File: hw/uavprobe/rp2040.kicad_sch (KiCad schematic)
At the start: 44 parts, among them IC1 UCLAMP3306P.TCT, SW1 SW_Push, U1 W25Q16JVSS, U2 NCP1117-5.0_SOT223, U3 RP2040, U4 TJA1051T-3, U5 TJA1051T-3, Y1 ABLS-12.000MHZ-B4-T

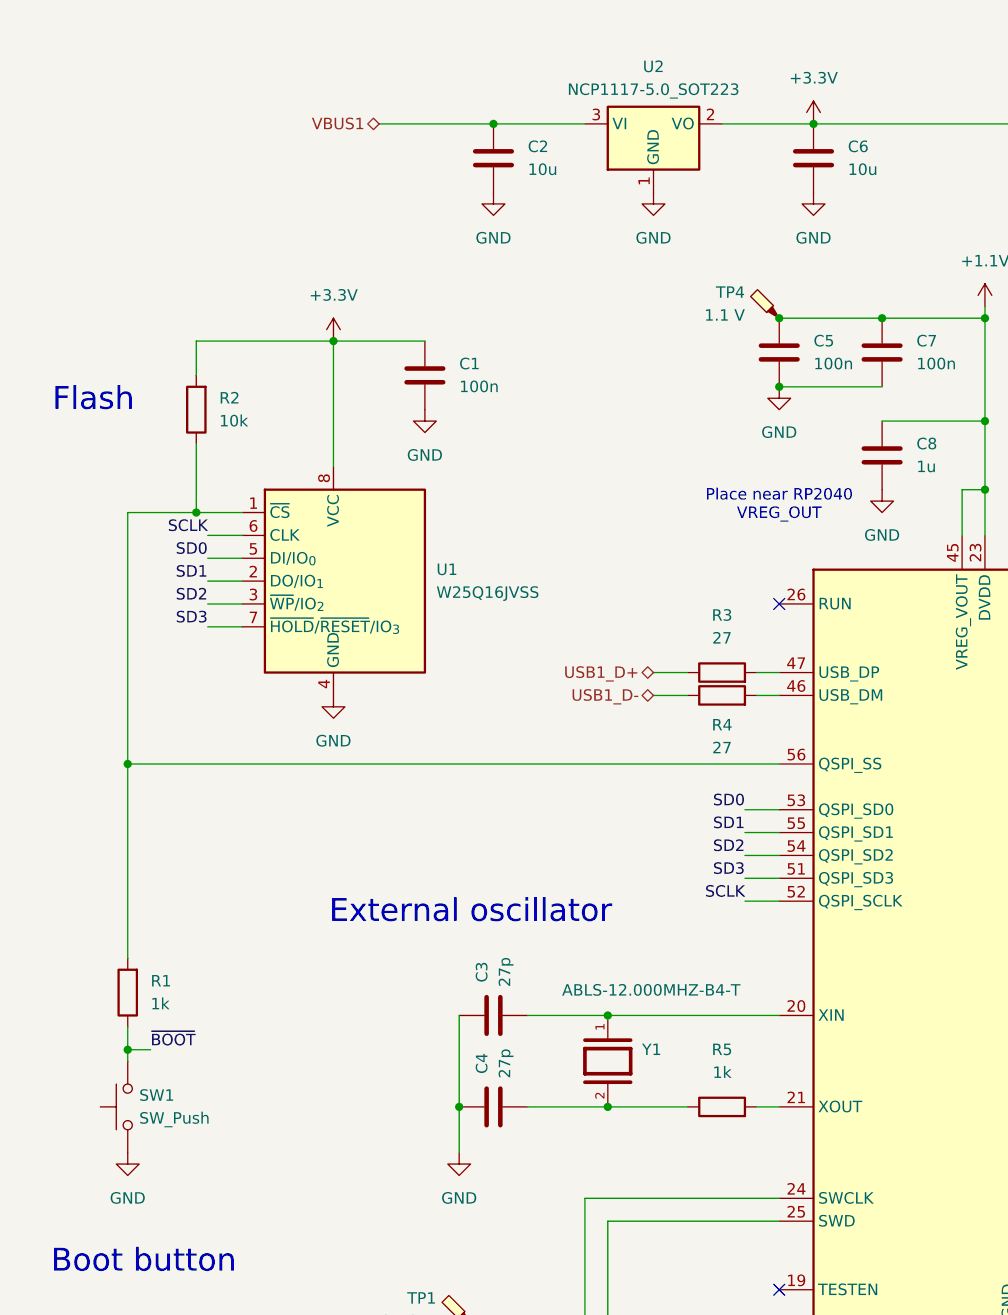
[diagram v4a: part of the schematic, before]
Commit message: ERC pass
Footprint and symbol copy editing warnings left
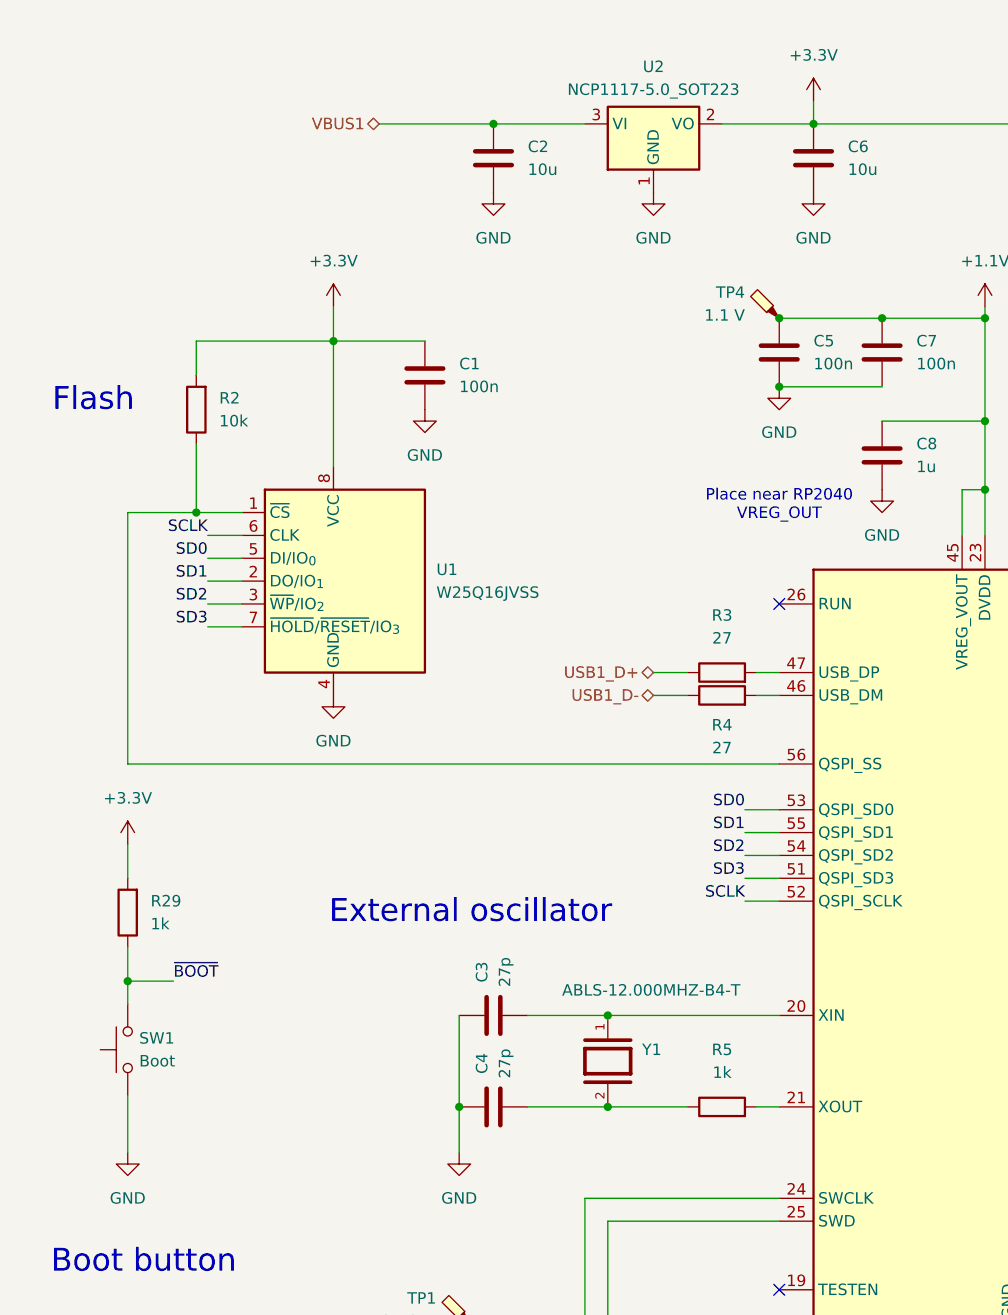
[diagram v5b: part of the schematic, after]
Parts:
- removed R1: 1k, symbol Device:R
- added R29: 1k, symbol Device:R
- SW1: value SW_Push -> Boot
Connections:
- net +3.3V: now also R29.2
- net ~{BOOT}: now also R29.1
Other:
- moved on the sheet: SW1
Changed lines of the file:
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@@
 	)
 	(junction
-		(at 25.4 99.06)
-		(diameter 0)
-		(color 0 0 0 0)
-	)
-	(junction
 		(at 120.65 68.58)
 		(diameter 0)
@@
 	)
 	(junction
+		(at 25.4 123.19)
+		(diameter 0)
+		(color 0 0 0 0)
+	)
+	(junction
 		(at 101.6 27.94)
 		(diameter 0)
@@
 	)
 	(junction
-		(at 25.4 130.81)
-		(diameter 0)
-		(color 0 0 0 0)
-	)
-	(junction
 		(at 151.13 57.15)
 		(diameter 0)
@@
 	(wire
 		(pts
-			(xy 25.4 130.81) (xy 25.4 132.08)
+			(xy 62.23 127) (xy 62.23 137.16)
 		)
 		(stroke
@@
 	(wire
 		(pts
-			(xy 62.23 127) (xy 62.23 137.16)
+			(xy 120.65 48.26) (xy 120.65 49.53)
 		)
 		(stroke
@@
 	(wire
 		(pts
-			(xy 120.65 48.26) (xy 120.65 49.53)
+			(xy 162.56 49.53) (xy 173.99 49.53)
 		)
 		(stroke
@@
 	(wire
 		(pts
-			(xy 162.56 49.53) (xy 173.99 49.53)
+			(xy 97.79 147.32) (xy 76.2 147.32)
 		)
 		(stroke
@@
 	(wire
 		(pts
-			(xy 97.79 147.32) (xy 76.2 147.32)
+			(xy 162.56 57.15) (xy 173.99 57.15)
 		)
 		(stroke
@@
 	(wire
 		(pts
-			(xy 25.4 99.06) (xy 25.4 120.65)
+			(xy 101.6 25.4) (xy 101.6 27.94)
 		)
 		(stroke
@@
 	(wire
 		(pts
-			(xy 162.56 57.15) (xy 173.99 57.15)
+			(xy 246.38 101.6) (xy 266.7 101.6)
 		)
 		(stroke
@@
 	(wire
 		(pts
-			(xy 246.38 101.6) (xy 266.7 101.6)
+			(xy 69.85 127) (xy 78.74 127)
 		)
 		(stroke
@@
 	(wire
 		(pts
-			(xy 69.85 127) (xy 78.74 127)
+			(xy 25.4 135.89) (xy 25.4 142.24)
 		)
 		(stroke
@@
 	(wire
 		(pts
+			(xy 48.26 48.26) (xy 48.26 52.07)
+		)
+		(stroke
+			(width 0)
+			(type default)
+		)
+	)
+	(wire
+		(pts
 			(xy 151.13 49.53) (xy 162.56 49.53)
 		)
@@
 	(wire
 		(pts
+			(xy 25.4 123.19) (xy 25.4 119.38)
+		)
+		(stroke
+			(width 0)
+			(type default)
+		)
+	)
+	(wire
+		(pts
+			(xy 25.4 111.76) (xy 25.4 107.95)
+		)
+		(stroke
+			(width 0)
+			(type default)
+		)
+	)
+	(wire
+		(pts
 			(xy 95.25 88.9) (xy 97.79 88.9)
 		)
@@
 	(wire
 		(pts
-			(xy 25.4 128.27) (xy 25.4 130.81)
-		)
-		(stroke
-			(width 0)
-			(type default)
-		)
-	)
-	(wire
-		(pts
 			(xy 196.85 137.16) (xy 201.93 137.16)
 		)
@@
 	(wire
 		(pts
-			(xy 27.94 130.81) (xy 25.4 130.81)
-		)
-		(stroke
-			(width 0)
-			(type default)
-		)
-	)
-	(wire
-		(pts
 			(xy 95.25 137.16) (xy 97.79 137.16)
 		)
@@
 	(wire
 		(pts
+			(xy 25.4 125.73) (xy 25.4 123.19)
+		)
+		(stroke
+			(width 0)
+			(type default)
+		)
+	)
+	(wire
+		(pts
 			(xy 241.3 86.36) (xy 246.38 86.36)
 		)
@@
 	(wire
 		(pts
+			(xy 25.4 123.19) (xy 30.48 123.19)
+		)
+		(stroke
+			(width 0)
+			(type default)
+		)
+	)
+	(wire
+		(pts
 			(xy 139.7 57.15) (xy 151.13 57.15)
 		)
@@
 		)
 	)
-	(label "~{BOOT}"
-		(at 27.94 130.81 0)
-		(effects
-			(font
-				(size 1.27 1.27)
-			)
-			(justify left bottom)
-		)
-	)
 	(label "SD0"
 		(at 34.29 76.2 180)
@@
 		)
 	)
+	(label "~{BOOT}"
+		(at 30.48 123.19 0)
+		(effects
+			(font
+				(size 1.27 1.27)
+			)
+			(justify left bottom)
+		)
+	)
 	(label "SD0"
 		(at 93.98 104.14 180)
@@
 	(symbol
 		(lib_id "power:+3.3V")
-		(at 48.26 52.07 0)
+		(at 48.26 48.26 0)
 		(unit 1)
 		(exclude_from_sim no)
@@
 		(fields_autoplaced yes)
 		(property "Reference" "#PWR02"
-			(at 48.26 55.88 0)
+			(at 48.26 52.07 0)
 			(effects
 				(font
@@
 		)
 		(property "Value" "+3.3V"
-			(at 48.26 46.99 0)
+			(at 48.26 43.18 0)
 			(effects
 				(font
@@
 		)
 		(property "Footprint" ""
-			(at 48.26 52.07 0)
+			(at 48.26 48.26 0)
 			(effects
 				(font
@@
 		)
 		(property "Datasheet" ""
-			(at 48.26 52.07 0)
+			(at 48.26 48.26 0)
 			(effects
 				(font
@@
 		)
 		(property "Description" "Power symbol creates a global label with name \"+3.3V\""
-			(at 48.26 52.07 0)
+			(at 48.26 48.26 0)
 			(effects
 				(font
@@
 	(symbol
 		(lib_id "power:+3.3V")
-		(at 101.6 27.94 0)
+		(at 101.6 25.4 0)
 		(unit 1)
 		(exclude_from_sim no)
@@
 		(dnp no)
 		(property "Reference" "#PWR010"
-			(at 101.6 31.75 0)
+			(at 101.6 29.21 0)
 			(effects
 				(font
@@
 		)
 		(property "Value" "+3.3V"
-			(at 101.6 22.86 0)
+			(at 101.6 20.32 0)
 			(effects
 				(font
@@
 		)
 		(property "Footprint" ""
-			(at 101.6 27.94 0)
+			(at 101.6 25.4 0)
 			(effects
 				(font
@@
 		)
 		(property "Datasheet" ""
-			(at 101.6 27.94 0)
+			(at 101.6 25.4 0)
 			(effects
 				(font
@@
 		)
 		(property "Description" "Power symbol creates a global label with name \"+3.3V\""
-			(at 101.6 27.94 0)
+			(at 101.6 25.4 0)
 			(effects
 				(font
@@
 	)
 	(symbol
+		(lib_id "power:+3.3V")
+		(at 25.4 107.95 0)
+		(unit 1)
+		(exclude_from_sim no)
+		(in_bom yes)
+		(on_board yes)
+		(dnp no)
+		(fields_autoplaced yes)
+		(property "Reference" "#PWR062"
+			(at 25.4 111.76 0)
+			(effects
+				(font
+					(size 1.27 1.27)
+				)
+				(hide yes)
+			)
+		)
+		(property "Value" "+3.3V"
+			(at 25.4 102.87 0)
+			(effects
+				(font
+					(size 1.27 1.27)
+				)
+			)
+		)
+		(property "Footprint" ""
+			(at 25.4 107.95 0)
+			(effects
+				(font
+					(size 1.27 1.27)
+				)
+				(hide yes)
+			)
+		)
+		(property "Datasheet" ""
+			(at 25.4 107.95 0)
+			(effects
+				(font
+					(size 1.27 1.27)
+				)
+				(hide yes)
+			)
+		)
+		(property "Description" "Power symbol creates a global label with name \"+3.3V\""
+			(at 25.4 107.95 0)
+			(effects
+				(font
+					(size 1.27 1.27)
+				)
+				(hide yes)
+			)
+		)
+		(pin "1"
+		)
+		(instances
+			(project "uavprobe"
+				(path "/e4efab0a-eb38-47b4-a7c8-7fdbedea4819/b637890e-36cc-449d-9355-32fb577ea192"
+					(reference "#PWR062")
+					(unit 1)
+				)
+			)
+		)
+	)
+	(symbol
 		(lib_id "power:GND")
 		(at 214.63 149.86 0)
@@
 	(symbol
 		(lib_id "Device:R")
-		(at 25.4 124.46 180)
+		(at 25.4 115.57 180)
 		(unit 1)
 		(exclude_from_sim no)
@@
 		(dnp no)
 		(fields_autoplaced yes)
-		(property "Reference" "R1"
-			(at 27.94 123.1899 0)
+		(property "Reference" "R29"
+			(at 27.94 114.2999 0)
 			(effects
 				(font
@@
 		)
 		(property "Value" "1k"
-			(at 27.94 125.7299 0)
+			(at 27.94 116.8399 0)
 			(effects
 				(font
@@
 		)
 		(property "Footprint" ""
-			(at 27.178 124.46 90)
+			(at 27.178 115.57 90)
 			(effects
 				(font
@@
 		)
 		(property "Datasheet" "~"
-			(at 25.4 124.46 0)
+			(at 25.4 115.57 0)
 			(effects
 				(font
@@
 		)
 		(property "Description" "Resistor"
-			(at 25.4 124.46 0)
+			(at 25.4 115.57 0)
 			(effects
 				(font
@@
 			(project "uavprobe"
 				(path "/e4efab0a-eb38-47b4-a7c8-7fdbedea4819/b637890e-36cc-449d-9355-32fb577ea192"
-					(reference "R1")
+					(reference "R29")
 					(unit 1)
 				)
@@
 	(symbol
 		(lib_id "Switch:SW_Push")
-		(at 25.4 137.16 90)
+		(at 25.4 130.81 90)
 		(unit 1)
 		(exclude_from_sim no)
@@
 		(fields_autoplaced yes)
 		(property "Reference" "SW1"
-			(at 26.67 135.8899 90)
+			(at 26.67 129.5399 90)
 			(effects
 				(font
@@
 			)
 		)
-		(property "Value" "SW_Push"
-			(at 26.67 138.4299 90)
+		(property "Value" "Boot"
+			(at 26.67 132.0799 90)
 			(effects
 				(font
@@
 		)
 		(property "Footprint" ""
-			(at 20.32 137.16 0)
+			(at 20.32 130.81 0)
 			(effects
 				(font
@@
 		)
 		(property "Datasheet" "~"
-			(at 20.32 137.16 0)
+			(at 20.32 130.81 0)
 			(effects
 				(font
@@
 		)
 		(property "Description" "Push button switch, generic, two pins"
-			(at 25.4 137.16 0)
+			(at 25.4 130.81 0)
 			(effects
 				(font

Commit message: Footprint/MPN assignment pass
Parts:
- C1, C10, C11, C12, C13, C14, C15, C16, C17, C18, C19, C2, C20, C3, C4, C5, C6, C7, C8, C9: footprint (none) -> Capacitor_SMD:C_0402_1005Metric
- D1, D2: MPN (none) -> NUP2105L
- IC1: footprint SON50P160X160X65-7N -> Import:SON50P160X160X65-7N; MPN (none) -> UCLAMP3306P.TCT; Manufacturer_Part_Number UCLAMP3306P.TCT -> (none)
- R2, R29, R3, R4, R5, R6, R7, R8, R9: footprint (none) -> Resistor_SMD:R_0402_1005Metric
- SW1: footprint (none) -> Button_Switch_SMD:SW_SPST_B3U-1000P; MPN (none) -> SW_SPST_B3U-1000P
- TP1, TP2, TP3, TP4, TP5: footprint (none) -> TestPoint:TestPoint_Pad_D1.5mm
- U1: MPN (none) -> W25Q16JVSS
- U2: MPN (none) -> NCP1117-5.0_SOT223
- U3: MPN (none) -> SC0914
- U4, U5: MPN (none) -> TJA1051T-3
- Y1: footprint ABLS-12.000MHZ-B4-T:XTAL_ABLS-12.000MHZ-B4-T -> Import:XTAL_ABLS-12.000MHZ-B4-T; MP ABLS-12.000MHZ-B4-T -> (none); MPN (none) -> ABLS-12.000MHZ-B4-T
